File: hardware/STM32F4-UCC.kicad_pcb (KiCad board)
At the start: 2 copper layers, 18 parts, among them P1 Con P1, P2 Con P2

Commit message: Terminado el esquematico, iniciado el PCB
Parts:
- added C1, C2: 47pF, Capacitors_SMD:c_1206, F.Cu at (148.5, 105.0)
- added C10: 10uF, Capacitors_ThroughHole:Capacitor5x11RM2.5, F.Cu at (148.5, 105.0)
- added C11, C12, C15, C16, C17, C19, C21, C22, C23, C24, C3, C5, C6, C7, C8, C9: 100nF, Capacitors_SMD:c_1206, F.Cu at (148.5, 105.0)
- added C13, C20, C4: 4.7uF, Capacitors_ThroughHole:Capacitor5x11RM2.5, F.Cu at (148.5, 105.0)
- added C14: 1uF, Capacitors_ThroughHole:Capacitor5x11RM2.5, F.Cu at (148.5, 105.0)
- added C18: 10nf, Capacitors_SMD:c_1206, F.Cu at (148.5, 105.0)
- added D10: TX, LEDs:LED-0805, F.Cu at (148.5, 105.0)
- added D11: POWER, LEDs:LED-0805, F.Cu at (148.5, 105.0)
- added D9: RX, LEDs:LED-0805, F.Cu at (148.5, 105.0)
- added L1: MI0805K601R-10, Resistors_SMD:Resistor_SMD0805_ReflowWave, F.Cu at (148.5, 105.0)
- added Q1: IRLML6402, SMD_Packages:SOT-23, F.Cu at (148.5, 105.0)
- added R10, R11, R12, R34, R62, R63, R9: 10k, Resistors_SMD:Resistor_SMD1206_ReflowWave, F.Cu at (148.5, 105.0)
- added R13, R14, R15, R16, R17, R21, R22, R37, R43, R48: 330, Resistors_SMD:Resistor_SMD1206_ReflowWave, F.Cu at (148.5, 105.0)
- added R18, R19: 27, Resistors_SMD:Resistor_SMD1206_ReflowWave, F.Cu at (148.5, 105.0)
- added R20: 1k, Resistors_SMD:Resistor_SMD1206_ReflowWave, F.Cu at (148.5, 105.0)
- added R23, R25, R28: 240, Resistors_SMD:Resistor_SMD1206_ReflowWave, F.Cu at (148.5, 105.0)
- added R24: 470, Resistors_SMD:Resistor_SMD1206_ReflowWave, F.Cu at (148.5, 105.0)
- added R26, R29: 560, Resistors_SMD:Resistor_SMD1206_ReflowWave, F.Cu at (148.5, 105.0)
- added R27, R30: 1100, Resistors_SMD:Resistor_SMD1206_ReflowWave, F.Cu at (148.5, 105.0)
- added R31, R32, R33, R44: 150, Resistors_SMD:Resistor_SMD1206_ReflowWave, F.Cu at (148.5, 105.0)
- added R35, R36, R38, R39: 2.2k, Resistors_SMD:Resistor_SMD1206_ReflowWave, F.Cu at (148.5, 105.0)
- added R40: 4.7k, Resistors_SMD:Resistor_SMD1206_ReflowWave, F.Cu at (148.5, 105.0)
- added R41, R42, R45, R46, R47: 18, Resistors_SMD:Resistor_SMD1206_ReflowWave, F.Cu at (148.5, 105.0)
- added R49: 100k, Resistors_SMD:Resistor_SMD1206_ReflowWave, F.Cu at (148.5, 105.0)
- added R50, R51, R52, R53, R54, R55: 47K, Resistors_SMD:Resistor_SMD1206_ReflowWave, F.Cu at (148.5, 105.0)
- added R56, R57, R58, R59, R60, R61: 22, Resistors_SMD:Resistor_SMD1206_ReflowWave, F.Cu at (148.5, 105.0)
- added U2: FT230X, Housings_SSOP:SSOP-16, F.Cu at (148.5, 105.0)
- added U4: MSP1825S-3302E, SMD_Packages:SOT-223, F.Cu at (148.5, 105.0)
- R1, R2, R3, R4, R5, R6, R7, R8: value R -> 330; footprint Resistors_SMD:Resistor_SMD0805_ReflowWave -> Resistors_SMD:Resistor_SMD1206_ReflowWave
- moved P1 64.7 mm to (148.5, 105.0), turned to 0 degrees
- moved D1 42.9 mm to (148.5, 105.0)
- moved D2 42.9 mm to (148.5, 105.0)
- moved D3 42.9 mm to (148.5, 105.0)
- moved D4 42.9 mm to (148.5, 105.0)
- moved D5 42.9 mm to (148.5, 105.0)
- moved D6 42.9 mm to (148.5, 105.0)
- moved D7 42.9 mm to (148.5, 105.0)
- moved D8 42.9 mm to (148.5, 105.0)
- moved R1 42.9 mm to (148.5, 105.0)
- moved R2 42.9 mm to (148.5, 105.0)
- moved R3 42.9 mm to (148.5, 105.0)
- moved R4 42.9 mm to (148.5, 105.0)
- moved R5 42.9 mm to (148.5, 105.0)
- moved R6 42.9 mm to (148.5, 105.0)
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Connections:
- net +3.3V renamed /SD-Card/VCC_SD
- net /PA1 renamed /Ethernet/OSCIN
- net /PA2 renamed /Ethernet/MDIO
- net /PB11 renamed /Ethernet/TX_EN
- net /PB12 renamed /Ethernet/TXD0
- net /PB13 renamed /Ethernet/TXD1
- net /PB7 renamed /VGA/VGA_HS
- net /PB8 renamed /VGA/VGA_VS
- net /PC1 renamed /Ethernet/MDC
- net /PC4 renamed /Ethernet/RXD0
- net /PC5 renamed /Ethernet/RXD1
- D1 pad 1: Net-(D1-Pad1) -> /PD0
- D2 pad 1: Net-(D2-Pad1) -> /PD1
- D3 pad 1: Net-(D3-Pad1) -> /PD2
- D4 pad 1: Net-(D4-Pad1) -> /PD3
- D5 pad 1: Net-(D5-Pad1) -> /PD6
- D6 pad 1: Net-(D6-Pad1) -> /PD7
- D7 pad 1: Net-(D7-Pad1) -> /PD10
- D8 pad 1: Net-(D8-Pad1) -> /PD11
- P1 pad 15: /PA5 -> /Ethernet/NRST
- P1 pad 17: /PA7 -> /Ethernet/CRS_DV
- P1 pad 25: /PE7 -> /SD-Card/Dat3/CS
- P1 pad 26: /PE8 -> /VGA/VGA_B0
- P1 pad 27: /PE9 -> /VGA/VGA_B1
- P1 pad 28: /PE10 -> /VGA/VGA_G0
- P1 pad 29: /PE11 -> /VGA/VGA_G1
- P1 pad 30: /PE12 -> /VGA/VGA_G2
- P1 pad 31: /PE13 -> /VGA/VGA_R0
- P1 pad 32: /PE14 -> /VGA/VGA_R1
- P1 pad 33: /PE15 -> /VGA/VGA_R2
- P1 pad 34: /PB10 -> /SD-Card/CLK/SCK
- P1 pad 38: /PB14 -> /SD-Card/Dat0/MISO
- P1 pad 39: /PB15 -> /SD-Card/CMD/MOSI
- P1 pad 40: /PD8 -> /USB-Serie/RX
- P1 pad 41: /PD9 -> /USB-Serie/TX

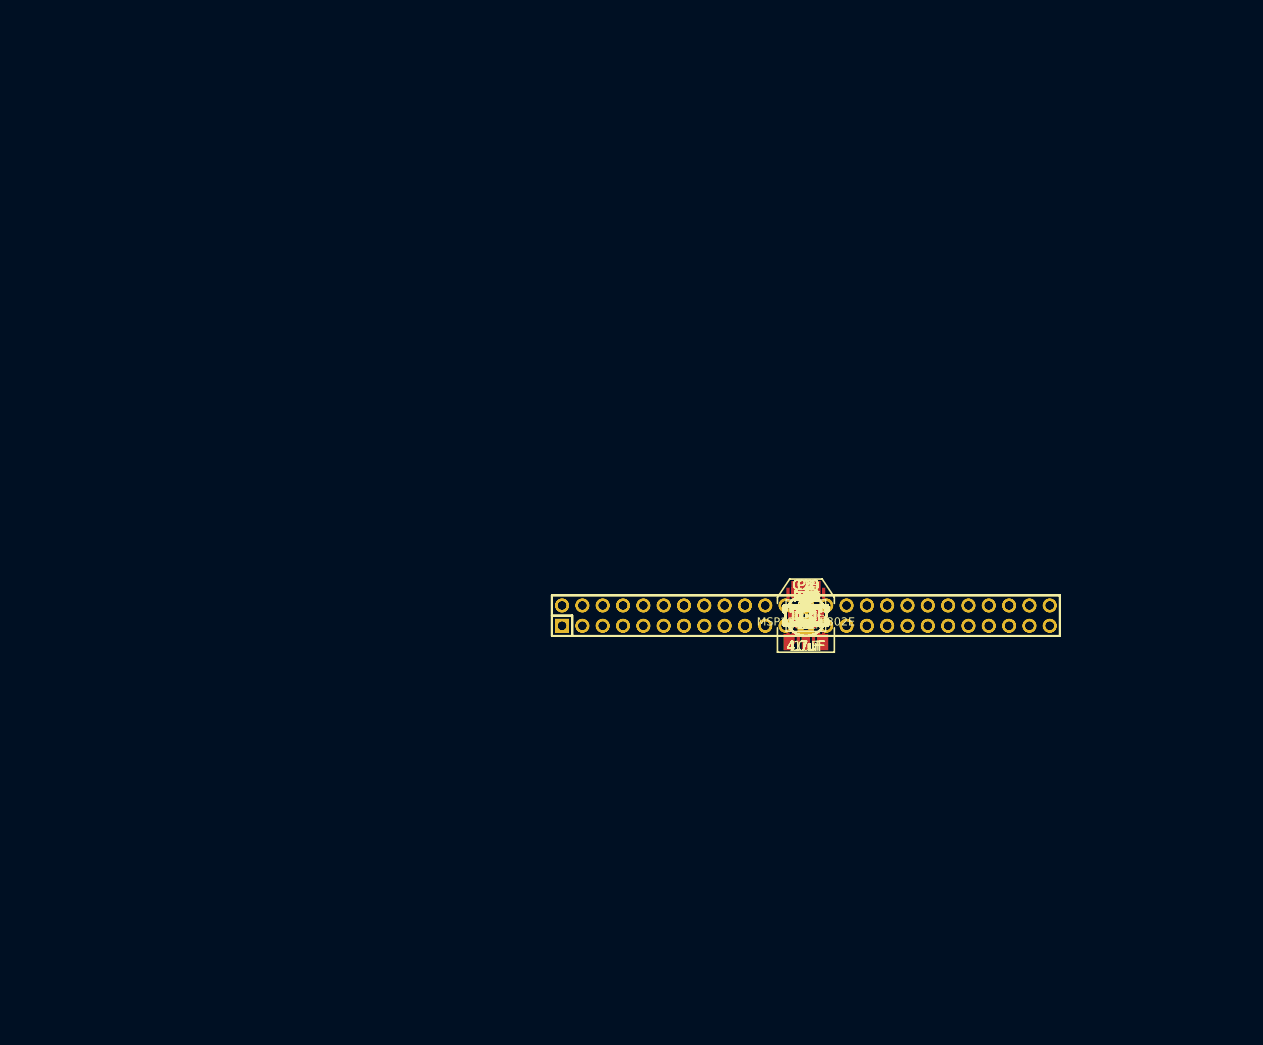
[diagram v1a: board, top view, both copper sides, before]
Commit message: Terminado el Routeo de la Placa
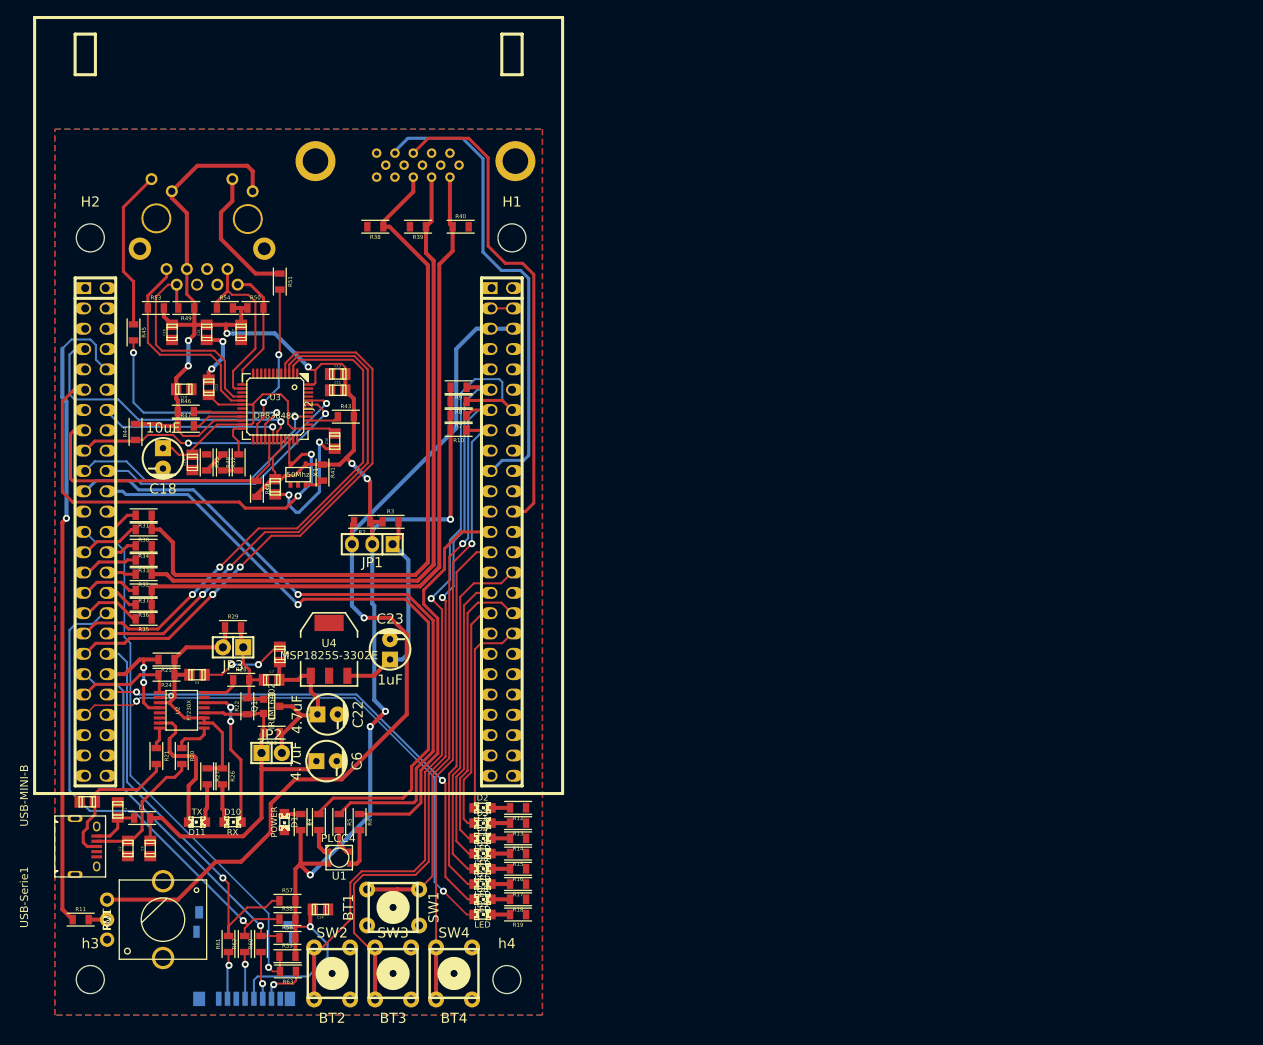
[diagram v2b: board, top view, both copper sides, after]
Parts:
- removed C20: 4.7uF, Capacitors_ThroughHole:Capacitor5x11RM2.5
- removed C9: 100nF, Capacitors_SMD:c_1206
- removed P1: Con P1, Pin_Headers:Pin_Header_Straight_2x25
- removed P2: Con P2, Pin_Headers:Pin_Header_Straight_2x25
- added H1: MountingHole_3-5mm_RevA_Date21Jun2010, Mounting_Holes:MountingHole_3-5mm, F.Cu at (111.8, 57.8)
- added H2: MountingHole_3-5mm_RevA_Date21Jun2010, Mounting_Holes:MountingHole_3-5mm, F.Cu at (59.1, 57.8)
- added J1: DB15, w_conn_pc:DB_15F-VGA, B.Cu at (99.7, 45.7)
- added J2: STM32F4_Discovery_Header, w_Connectors:stm32f4_discovery_header, F.Cu at (85.1, 78.7)
- added J3: RJ45-TRANSFO_W, w_Connectors:RJ45, B.Cu at (73.0, 44.5)
- added JP1: Alimentacion, Pin_Headers:Pin_Header_Straight_1x03, F.Cu at (94.3, 96.1)
- added JP2: Alim Ext, Pin_Headers:Pin_Header_Straight_1x02, F.Cu at (81.7, 122.2)
- added JP3: G_MOS, Pin_Headers:Pin_Header_Straight_1x02, F.Cu at (76.9, 109.0)
- added RV1: POT, w_Connectors:POTE, F.Cu at (61.2, 143.0)
- added SW1: BT1, w_switch:PCB_PUSH, F.Cu at (96.9, 141.5)
- added SW2: BT2, w_switch:PCB_PUSH, F.Cu at (89.3, 149.7)
- added SW3: BT3, w_switch:PCB_PUSH, F.Cu at (96.9, 149.7)
- added SW4: BT4, w_switch:PCB_PUSH, F.Cu at (104.5, 149.7)
- added U1: PLCC4, w_Connectors:PLCC4, F.Cu at (90.2, 135.3)
- added U3: DP83848C, w_smd_lqfp:lqfp48, F.Cu at (82.2, 78.9)
- added U5: microSD, w_Connectors:microSD, B.Cu at (82.8, 152.0)
- added USB-Serie1: USB-MINI-B, w_Connectors:Micro_USB_type_B, F.Cu at (57.1, 133.9)
- added X1: 50Mhz, SMD_Packages:SOT-23-5, F.Cu at (85.0, 87.4)
- added h3: MountingHole_3-5mm_RevA_Date21Jun2010, Mounting_Holes:MountingHole_3-5mm, F.Cu at (59.1, 150.5)
- added h4: MountingHole_3-5mm_RevA_Date21Jun2010, Mounting_Holes:MountingHole_3-5mm, F.Cu at (111.1, 150.5)
- C1: value 47pF -> 10nf; footprint Capacitors_SMD:c_1206 -> Capacitors_SMD:c_0805
- C10: value 10uF -> 100nF; footprint Capacitors_ThroughHole:Capacitor5x11RM2.5 -> Capacitors_SMD:c_0805
- C11, C12, C15, C16, C17, C19, C2, C21, C24, C5, C7, C8: footprint Capacitors_SMD:c_1206 -> Capacitors_SMD:c_0805
- C13, C4: value 4.7uF -> 100nF; footprint Capacitors_ThroughHole:Capacitor5x11RM2.5 -> Capacitors_SMD:c_0805
- C14: value 1uF -> 100nF; footprint Capacitors_ThroughHole:Capacitor5x11RM2.5 -> Capacitors_SMD:c_0805
- C18: value 10nf -> 10uF; footprint Capacitors_SMD:c_1206 -> Capacitors_ThroughHole:Capacitor5x11RM2.5
- C22, C6: value 100nF -> 4.7uF; footprint Capacitors_SMD:c_1206 -> Capacitors_ThroughHole:Capacitor5x11RM2.5
- C23: value 100nF -> 1uF; footprint Capacitors_SMD:c_1206 -> Capacitors_ThroughHole:Capacitor5x11RM2.5
- C3: value 100nF -> 47pF; footprint Capacitors_SMD:c_1206 -> Capacitors_SMD:c_0805
- D1: value LED -> POWER
- D10: value TX -> RX
- D11: value POWER -> TX
- D2: value LED -> L1
- D3: value LED -> L2
- D9: value RX -> LED
- L1: footprint Resistors_SMD:Resistor_SMD0805_ReflowWave -> Resistors_SMD:R_0805
- Q1: footprint SMD_Packages:SOT-23 -> SMD_Packages:SOT-23-GDS
- R1, R10, R13, R14, R15, R16, R17, R4, R5, R6, R60, R61, R9: footprint Resistors_SMD:Resistor_SMD1206_ReflowWave -> Resistors_SMD:R_0805
- R11, R12: value 10k -> 330; footprint Resistors_SMD:Resistor_SMD1206_ReflowWave -> Resistors_SMD:R_0805
- R18, R19: value 27 -> 330; footprint Resistors_SMD:Resistor_SMD1206_ReflowWave -> Resistors_SMD:R_0805
- R2, R3: value 330 -> 0; footprint Resistors_SMD:Resistor_SMD1206_ReflowWave -> Resistors_SMD:R_0805
- R20: value 1k -> 27; footprint Resistors_SMD:Resistor_SMD1206_ReflowWave -> Resistors_SMD:R_0805
- R21: value 330 -> 27; footprint Resistors_SMD:Resistor_SMD1206_ReflowWave -> Resistors_SMD:R_0805
- R22: value 330 -> 100k; footprint Resistors_SMD:Resistor_SMD1206_ReflowWave -> Resistors_SMD:R_0805
- R23: value 240 -> 0; footprint Resistors_SMD:Resistor_SMD1206_ReflowWave -> Resistors_SMD:R_0805
- R24: value 470 -> 10k; footprint Resistors_SMD:Resistor_SMD1206_ReflowWave -> Resistors_SMD:R_0805
- R25: value 240 -> 10k; footprint Resistors_SMD:Resistor_SMD1206_ReflowWave -> Resistors_SMD:R_0805
- R26: value 560 -> 330; footprint Resistors_SMD:Resistor_SMD1206_ReflowWave -> Resistors_SMD:R_0805
- R27: value 1100 -> 330; footprint Resistors_SMD:Resistor_SMD1206_ReflowWave -> Resistors_SMD:R_0805
- R28: value 240 -> 1k; footprint Resistors_SMD:Resistor_SMD1206_ReflowWave -> Resistors_SMD:R_0805
- R29: value 560 -> 0; footprint Resistors_SMD:Resistor_SMD1206_ReflowWave -> Resistors_SMD:R_0805
- R30: value 1100 -> 240; footprint Resistors_SMD:Resistor_SMD1206_ReflowWave -> Resistors_SMD:R_0805
- R31: value 150 -> 470; footprint Resistors_SMD:Resistor_SMD1206_ReflowWave -> Resistors_SMD:R_0805
- R32: value 150 -> 240; footprint Resistors_SMD:Resistor_SMD1206_ReflowWave -> Resistors_SMD:R_0805
- R33: value 150 -> 560; footprint Resistors_SMD:Resistor_SMD1206_ReflowWave -> Resistors_SMD:R_0805
- R34: value 10k -> 1100; footprint Resistors_SMD:Resistor_SMD1206_ReflowWave -> Resistors_SMD:R_0805
- R35: value 2.2k -> 240; footprint Resistors_SMD:Resistor_SMD1206_ReflowWave -> Resistors_SMD:R_0805
- R36: value 2.2k -> 560; footprint Resistors_SMD:Resistor_SMD1206_ReflowWave -> Resistors_SMD:R_0805
- R37: value 330 -> 1100; footprint Resistors_SMD:Resistor_SMD1206_ReflowWave -> Resistors_SMD:R_0805
- R38, R39: value 2.2k -> 150; footprint Resistors_SMD:Resistor_SMD1206_ReflowWave -> Resistors_SMD:R_0805
- R40: value 4.7k -> 150; footprint Resistors_SMD:Resistor_SMD1206_ReflowWave -> Resistors_SMD:R_0805
- R41: value 18 -> 1k; footprint Resistors_SMD:Resistor_SMD1206_ReflowWave -> Resistors_SMD:R_0805
- R42: value 18 -> 10k; footprint Resistors_SMD:Resistor_SMD1206_ReflowWave -> Resistors_SMD:R_0805
- R43: value 330 -> 2.2k; footprint Resistors_SMD:Resistor_SMD1206_ReflowWave -> Resistors_SMD:R_0805
- R44: value 150 -> 2.2k; footprint Resistors_SMD:Resistor_SMD1206_ReflowWave -> Resistors_SMD:R_0805
- R45: value 18 -> 330; footprint Resistors_SMD:Resistor_SMD1206_ReflowWave -> Resistors_SMD:R_0805
- R46, R47: value 18 -> 2.2k; footprint Resistors_SMD:Resistor_SMD1206_ReflowWave -> Resistors_SMD:R_0805
- R48: value 330 -> 4.7k; footprint Resistors_SMD:Resistor_SMD1206_ReflowWave -> Resistors_SMD:R_0805
- R49: value 100k -> 18; footprint Resistors_SMD:Resistor_SMD1206_ReflowWave -> Resistors_SMD:R_0805
- R50, R53, R54, R55: value 47K -> 18; footprint Resistors_SMD:Resistor_SMD1206_ReflowWave -> Resistors_SMD:R_0805
- R51: value 47K -> 330; footprint Resistors_SMD:Resistor_SMD1206_ReflowWave -> Resistors_SMD:R_0805
- R52: value 47K -> 150; footprint Resistors_SMD:Resistor_SMD1206_ReflowWave -> Resistors_SMD:R_0805
- R56, R57, R58, R59: value 22 -> 47K; footprint Resistors_SMD:Resistor_SMD1206_ReflowWave -> Resistors_SMD:R_0805
- R62, R63: value 10k -> 22; footprint Resistors_SMD:Resistor_SMD1206_ReflowWave -> Resistors_SMD:R_0805
- R7, R8: value 330 -> 10k; footprint Resistors_SMD:Resistor_SMD1206_ReflowWave -> Resistors_SMD:R_0805
- moved R11 98.3 mm to (57.8, 143.0)
- moved C3 92.8 mm to (58.7, 128.3)
- moved R45 91.2 mm to (64.5, 69.6), turned to 270 degrees
- moved R53 89.9 mm to (67.2, 66.5)
- moved C2 89.6 mm to (63.8, 134.1), turned to 90 degrees
- moved C1 89.4 mm to (62.5, 129.3), turned to 270 degrees
- moved C5 87.0 mm to (66.5, 134.1), turned to 90 degrees
- moved R44 86.9 mm to (64.7, 82.0), turned to 90 degrees
- moved C16 86.8 mm to (69.3, 69.6), turned to 90 degrees
- moved L1 86.7 mm to (65.5, 130.3)
- moved R49 86.5 mm to (71.1, 66.5), turned to 180 degrees
- moved R31 83.7 mm to (65.7, 92.5), turned to 180 degrees
- moved R30 83.5 mm to (65.7, 94.2), turned to 180 degrees
- moved R34 83.2 mm to (65.7, 96.3), turned to 180 degrees
- moved R33 83.1 mm to (65.7, 98.0), turned to 180 degrees
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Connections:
- C12 pad 1: +3.3V -> Net-(C10-Pad1)
- C13 pad 1: /USB-Serie/5v_USB -> +3.3V
- C14 pad 1: +3.3V -> Net-(C10-Pad1)
- C15 pad 1: /USB-Serie/5v_USB -> +3.3V
- C15 pad 2: Net-(C15-Pad2) -> GND
- C16 pad 1: /USB-Serie/5v_USB -> +3.3V
- C17 pad 1: /SD-Card/VCC_SD -> +3.3V
- C18 pad 1: Net-(C18-Pad1) -> Net-(C10-Pad1)
- C19 pad 1: Net-(C19-Pad1) -> +3.3V
- C22 pad 1: +3.3V -> /USB-Serie/5v_USB
- C23 pad 1: +3.3V -> /Fuente/3.3V_OUT
- C3 pad 1: /USB-Serie/3.3v_FT -> Net-(C3-Pad1)
- C4 pad 1: /USB-Serie/5v_USB -> /USB-Serie/3.3v_FT
- C5 pad 1: Net-(C10-Pad1) -> Net-(C5-Pad1)
- C6 pad 1: Net-(C10-Pad1) -> Net-(C5-Pad1)
- C7 pad 1: Net-(C10-Pad1) -> /USB-Serie/5v_USB
- C7 pad 2: GND -> Net-(C7-Pad2)
- C8 pad 1: +3.3V -> /USB-Serie/5v_USB
- D1 pad 1: /PD0 -> Net-(D1-Pad1)
- D1 pad 2: Net-(D1-Pad2) -> GND
- D11 pad 2: GND -> Net-(D11-Pad2)
- D2 pad 1: /PD1 -> /PD0
- D3 pad 1: /PD2 -> /PD1
- D4 pad 1: /PD3 -> /PD2
- D5 pad 1: /PD6 -> /PD3
- D6 pad 1: /PD7 -> /PD6
- D7 pad 1: /PD10 -> /PD7
- D8 pad 1: /PD11 -> /PD10
- D9 pad 1: Net-(D9-Pad1) -> /PD11
- L1 pad 1: Net-(C18-Pad1) -> Net-(C1-Pad1)
- L1 pad 2: Net-(C19-Pad1) -> Net-(C5-Pad1)
- R1 pad 1: GND -> Net-(D1-Pad1)
- R1 pad 2: Net-(D1-Pad2) -> +3.3V
- R10 pad 1: /PE5 -> /PE2
- R10 pad 2: /SD-Card/VCC_SD -> +3.3V
- R11 pad 1: /PE6 -> /PC2
- R11 pad 2: /SD-Card/VCC_SD -> Net-(R11-Pad2)
- R12 pad 1: /PE2 -> GND
- R12 pad 2: /SD-Card/VCC_SD -> Net-(D2-Pad2)
- R13 pad 2: Net-(R13-Pad2) -> Net-(D3-Pad2)
- R14 pad 2: Net-(R14-Pad2) -> Net-(D4-Pad2)
- R15 pad 2: Net-(R15-Pad2) -> Net-(D5-Pad2)
- R16 pad 1: /PC2 -> GND
- R16 pad 2: Net-(R16-Pad2) -> Net-(D6-Pad2)
- R17 pad 1: /PA3 -> GND
- R17 pad 2: Net-(R17-Pad2) -> Net-(D7-Pad2)
- R18 pad 1: Net-(R18-Pad1) -> GND
- R18 pad 2: Net-(C1-Pad1) -> Net-(D8-Pad2)
- R19 pad 1: Net-(R19-Pad1) -> GND
- R19 pad 2: Net-(C2-Pad1) -> Net-(D9-Pad2)
- R2 pad 1: GND -> +3.3V
- R2 pad 2: Net-(D2-Pad2) -> /3.3V_discovery
- R20 pad 2: Net-(C15-Pad2) -> Net-(C2-Pad1)
- R21 pad 1: /USB-Serie/3.3v_FT -> Net-(R21-Pad1)
- R21 pad 2: Net-(D9-Pad1) -> Net-(C3-Pad1)
- R22 pad 1: /USB-Serie/3.3v_FT -> Net-(C5-Pad1)
- R22 pad 2: Net-(D10-Pad1) -> Net-(C7-Pad2)
- R23 pad 1: Net-(J1-Pad3) -> /USB-Serie/5v_USB
- R23 pad 2: /VGA/VGA_B1 -> Net-(C5-Pad1)
- R24 pad 1: Net-(J1-Pad3) -> /USB-Serie/3.3v_FT
- R24 pad 2: /VGA/VGA_B0 -> /USB-Serie/TX
- R25 pad 1: Net-(J1-Pad2) -> /USB-Serie/3.3v_FT
- R25 pad 2: /VGA/VGA_G2 -> /USB-Serie/RX
- R26 pad 1: Net-(J1-Pad2) -> /USB-Serie/3.3v_FT
- R26 pad 2: /VGA/VGA_G1 -> Net-(D10-Pad1)
- R27 pad 1: Net-(J1-Pad2) -> /USB-Serie/3.3v_FT
- R27 pad 2: /VGA/VGA_G0 -> Net-(D11-Pad1)
- R28 pad 1: Net-(J1-Pad1) -> Net-(R28-Pad1)
- R28 pad 2: /VGA/VGA_R2 -> Net-(C7-Pad2)
- R29 pad 1: Net-(J1-Pad1) -> /USB-Serie/3.3v_FT
- R29 pad 2: /VGA/VGA_R1 -> Net-(C7-Pad2)
- R3 pad 1: GND -> +3.3V
- R3 pad 2: Net-(D3-Pad2) -> /Fuente/3.3V_OUT
- R30 pad 1: Net-(J1-Pad1) -> Net-(J1-Pad3)
- R30 pad 2: /VGA/VGA_R0 -> /VGA/VGA_B1
- R31 pad 2: GND -> /VGA/VGA_B0
- R32 pad 2: GND -> /VGA/VGA_G2
- R33 pad 1: Net-(J1-Pad1) -> Net-(J1-Pad2)
- R33 pad 2: GND -> /VGA/VGA_G1
- R34 pad 1: /Ethernet/NRST -> Net-(J1-Pad2)
- R34 pad 2: +3.3V -> /VGA/VGA_G0
- R35 pad 1: Net-(R35-Pad1) -> Net-(J1-Pad1)
- R35 pad 2: +3.3V -> /VGA/VGA_R2
- R36 pad 1: /Ethernet/CRS_DV -> Net-(J1-Pad1)
- R36 pad 2: +3.3V -> /VGA/VGA_R1
- R37 pad 1: Net-(J2-PadGK) -> Net-(J1-Pad1)
- R37 pad 2: Net-(R37-Pad2) -> /VGA/VGA_R0
- R38 pad 1: +3.3V -> Net-(J1-Pad3)
- R38 pad 2: Net-(R38-Pad2) -> GND
- R39 pad 1: +3.3V -> Net-(J1-Pad2)
- R39 pad 2: Net-(R39-Pad2) -> GND
- R4 pad 1: GND -> Net-(R4-Pad1)
- R4 pad 2: Net-(D4-Pad2) -> /PB0
- R40 pad 1: Net-(R40-Pad1) -> Net-(J1-Pad1)
- R40 pad 2: Net-(R40-Pad2) -> GND
- R42 pad 1: +3.3V -> /Ethernet/NRST
- R42 pad 2: Net-(J2-Pad6) -> +3.3V
- R43 pad 2: Net-(R43-Pad2) -> +3.3V
- R44 pad 1: Net-(R44-Pad1) -> /Ethernet/CRS_DV
- R44 pad 2: Net-(R40-Pad1) -> +3.3V
- R45 pad 2: +3.3V -> Net-(R45-Pad2)
- R46 pad 1: Net-(J2-Pad4) -> +3.3V
- R46 pad 2: +3.3V -> Net-(R46-Pad2)
- R47 pad 1: GND -> +3.3V
- R47 pad 2: Net-(R44-Pad1) -> Net-(R47-Pad2)
- R48 pad 1: Net-(D11-Pad1) -> Net-(R48-Pad1)
- R48 pad 2: +3.3V -> Net-(R48-Pad2)
- R49 pad 1: Net-(C19-Pad1) -> +3.3V
- R49 pad 2: Net-(C15-Pad2) -> Net-(J3-PadR2)
- R5 pad 1: GND -> /PB1
- R5 pad 2: Net-(D5-Pad2) -> Net-(R5-Pad2)
- R50 pad 1: /SD-Card/Dat0/MISO -> +3.3V
- R50 pad 2: /SD-Card/VCC_SD -> Net-(J3-PadR8)
- R51 pad 1: /SD-Card/CLK/SCK -> Net-(J3-PadL2)
- R51 pad 2: /SD-Card/VCC_SD -> Net-(R51-Pad2)
- R52 pad 1: /SD-Card/CMD/MOSI -> Net-(R52-Pad1)
- R52 pad 2: /SD-Card/VCC_SD -> Net-(R48-Pad1)
- R53 pad 1: /SD-Card/Dat3/CS -> Net-(J3-PadR1)
- R53 pad 2: /SD-Card/VCC_SD -> +3.3V
- R54 pad 1: Net-(R54-Pad1) -> Net-(J3-PadR7)
- R54 pad 2: /SD-Card/VCC_SD -> +3.3V
- R55 pad 1: Net-(R55-Pad1) -> GND
- R55 pad 2: /SD-Card/VCC_SD -> Net-(R52-Pad1)
- R56 pad 1: Net-(R56-Pad1) -> /SD-Card/CMD/MOSI
- R56 pad 2: Net-(R55-Pad1) -> +3.3V
- R57 pad 1: Net-(R57-Pad1) -> /SD-Card/Dat0/MISO
- R57 pad 2: /SD-Card/Dat0/MISO -> +3.3V
- R58 pad 1: Net-(R58-Pad1) -> /SD-Card/CLK/SCK
- R58 pad 2: /SD-Card/CLK/SCK -> +3.3V
- R59 pad 1: Net-(R59-Pad1) -> /SD-Card/Dat3/CS
- R59 pad 2: /SD-Card/CMD/MOSI -> +3.3V
- R6 pad 1: GND -> /PB4
- R6 pad 2: Net-(D6-Pad2) -> Net-(R6-Pad2)
- R60 pad 2: /SD-Card/Dat3/CS -> /SD-Card/CMD/MOSI
- R61 pad 2: Net-(R54-Pad1) -> /SD-Card/Dat0/MISO
- R62 pad 1: /USB-Serie/3.3v_FT -> Net-(R62-Pad1)
- R62 pad 2: /USB-Serie/TX -> /SD-Card/CLK/SCK
- R63 pad 1: /USB-Serie/3.3v_FT -> Net-(R63-Pad1)
- R63 pad 2: /USB-Serie/RX -> /SD-Card/Dat3/CS
- R7 pad 1: GND -> /PE4
- R7 pad 2: Net-(D7-Pad2) -> +3.3V
- R8 pad 1: GND -> /PE5
- R8 pad 2: Net-(D8-Pad2) -> +3.3V
- R9 pad 1: /PE4 -> /PE6
- R9 pad 2: /SD-Card/VCC_SD -> +3.3V
- U2 pad 12: Net-(C19-Pad1) -> Net-(C5-Pad1)
- U2 pad 14: Net-(D9-Pad2) -> Net-(D10-Pad2)
- U2 pad 15: Net-(U2-Pad15) -> (no net)
- U2 pad 16: Net-(R20-Pad1) -> Net-(R28-Pad1)
- U2 pad 2: Net-(U2-Pad2) -> (no net)
- U2 pad 6: Net-(U2-Pad6) -> (no net)
- U2 pad 7: Net-(D10-Pad2) -> Net-(D11-Pad2)
- U2 pad 8: Net-(R19-Pad1) -> Net-(R21-Pad1)
- U2 pad 9: Net-(R18-Pad1) -> Net-(R20-Pad1)
- U4 pad 3: +3.3V -> /Fuente/3.3V_OUT
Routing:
- net +3.3V: track 0.00 -> 260.8 mm, vias 0 -> 11
- net /3.3V_discovery: track 0.00 -> 115.9 mm, vias 0 -> 1
- net /PE5: track 0.00 -> 105.2 mm, vias 0 -> 1
- net /PE6: track 0.00 -> 94.0 mm, vias 0 -> 1
- net Net-(J1-Pad3): track 0.00 -> 94.0 mm
- net Net-(J1-Pad1): track 0.00 -> 90.6 mm
- net Net-(J1-Pad2): track 0.00 -> 89.1 mm
- net /PB1: track 0.00 -> 85.0 mm, vias 0 -> 1
- net /PB0: track 0.00 -> 82.5 mm, vias 0 -> 1
- net /PC2: track 0.00 -> 80.8 mm, vias 0 -> 1
- net /PE2: track 0.00 -> 78.2 mm, vias 0 -> 1
- net /PE4: track 0.00 -> 74.6 mm, vias 0 -> 1
- net /Ethernet/TXD1: track 0.00 -> 71.2 mm, vias 0 -> 2
- net /SD-Card/Dat3/CS: track 0.00 -> 69.0 mm, vias 0 -> 1
- net /PD11: track 0.00 -> 68.9 mm, vias 0 -> 2
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- added copper zone on B.Cu, net GND
- added copper zone on F.Cu, net GND
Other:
- net class Alimentacion added: clearance 0.2032, trace_width 0.381, via_dia 0.889, via_drill 0.635
- net class Default: clearance 0.254 -> 0.2032; trace_width 0.254 -> 0.2032
- rule trace_clearance: 0.254 -> 0.2032
- rule trace_min: 0.254 -> 0.2032

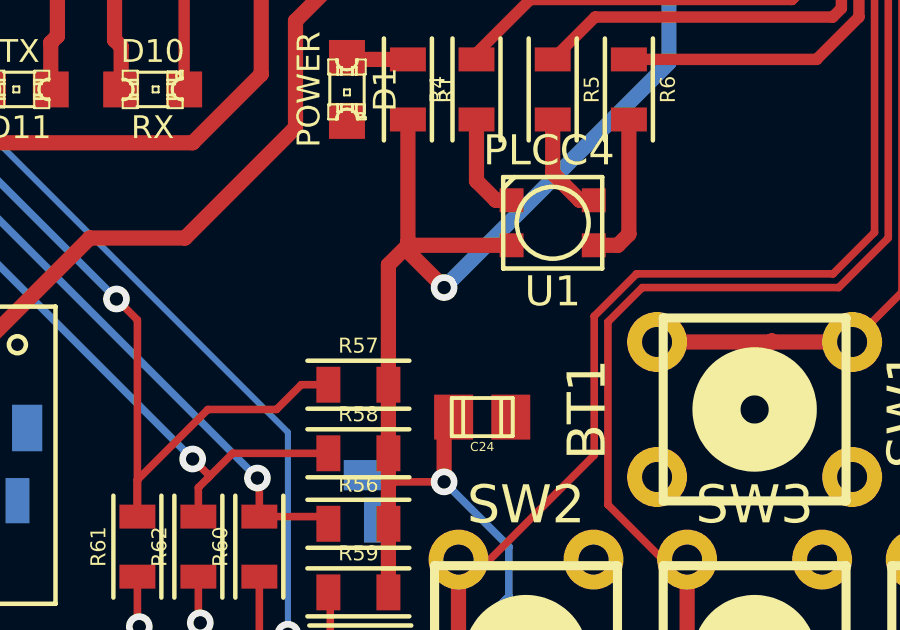
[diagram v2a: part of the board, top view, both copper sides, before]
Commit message: Se arreglo pista a via
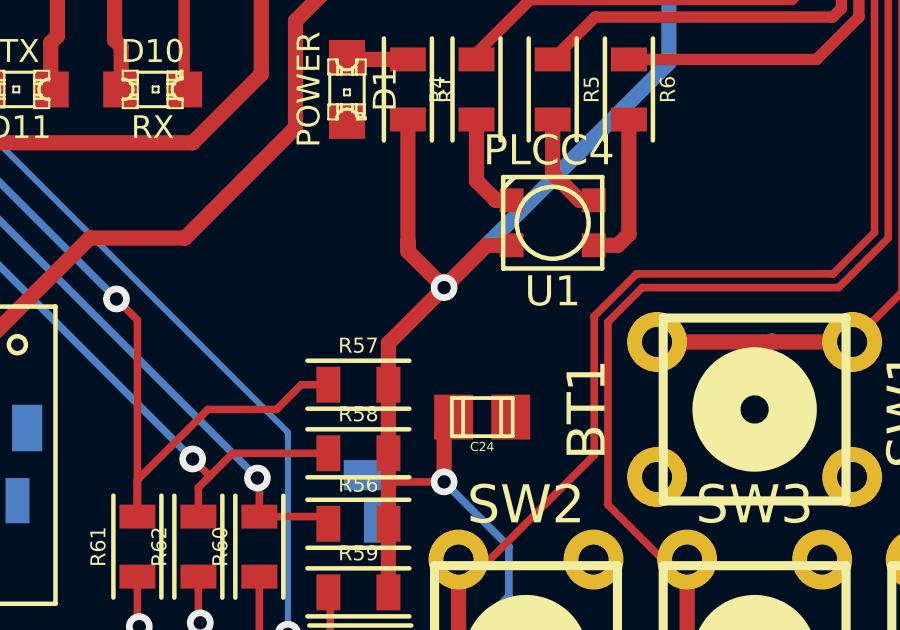
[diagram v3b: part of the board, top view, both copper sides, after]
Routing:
- net +3.3V: track 260.8 -> 259.2 mm
